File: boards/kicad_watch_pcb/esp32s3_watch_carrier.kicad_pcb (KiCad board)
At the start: 2 copper layers, 180 x 120 mm, 10 parts, among them J1 ESP32-S3 GPIO BUS, J2 ST7735 128x128, J3 I2S MIC, J4 MAX98357A, J5 MPU6050, J6 POWER, SW1 P4, SW2 P5, SW3 P6, SW4 P7

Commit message: Route KiCad watch signal traces
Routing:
- net GPIO12_TFT_SCK: track 0.00 -> 170.5 mm
- net GPIO15_TFT_LED: track 0.00 -> 155.0 mm
- net GPIO11_TFT_MOSI: track 0.00 -> 146.5 mm
- net GPIO8_TFT_RST: track 0.00 -> 135.5 mm
- net GPIO17_I2S_WS: track 0.00 -> 134.4 mm
- net GPIO16_I2S_BCLK: track 0.00 -> 134.4 mm
- net GPIO14_SPK_DIN: track 0.00 -> 96.4 mm
- net GPIO9_TFT_DC: track 0.00 -> 84.7 mm
- net GPIO10_TFT_CS: track 0.00 -> 84.7 mm
- net GPIO18_MIC_SD: track 0.00 -> 72.0 mm
- net GPIO42_MPU_SDA: track 0.00 -> 65.1 mm
- net GPIO41_MPU_SCL: track 0.00 -> 65.1 mm
- net GPIO13_MPU_INT: track 0.00 -> 65.1 mm
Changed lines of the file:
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@@
     (effects (font (size 0.9 0.9) (thickness 0.12)))
   )
+  (segment (start 96.00 61.02) (end 86.00 61.02) (width 0.25) (layer "B.Cu") (net 14))
+  (segment (start 86.00 61.02) (end 86.00 75.00) (width 0.25) (layer "B.Cu") (net 14))
+  (segment (start 86.00 75.00) (end 14.00 75.00) (width 0.25) (layer "B.Cu") (net 14))
+  (segment (start 14.00 75.00) (end 14.00 27.00) (width 0.25) (layer "B.Cu") (net 14))
+  (segment (start 14.00 27.00) (end 25.00 27.00) (width 0.25) (layer "B.Cu") (net 14))
+  (segment (start 96.00 55.94) (end 120.00 55.94) (width 0.25) (layer "F.Cu") (net 12))
+  (segment (start 120.00 55.94) (end 120.00 20.00) (width 0.25) (layer "F.Cu") (net 12))
+  (segment (start 120.00 20.00) (end 22.00 20.00) (width 0.25) (layer "F.Cu") (net 12))
+  (segment (start 22.00 20.00) (end 22.00 29.54) (width 0.25) (layer "F.Cu") (net 12))
+  (segment (start 22.00 29.54) (end 25.00 29.54) (width 0.25) (layer "F.Cu") (net 12))
+  (segment (start 96.00 53.40) (end 115.00 53.40) (width 0.25) (layer "F.Cu") (net 11))
+  (segment (start 115.00 53.40) (end 115.00 24.00) (width 0.25) (layer "F.Cu") (net 11))
+  (segment (start 115.00 24.00) (end 30.00 24.00) (width 0.25) (layer "F.Cu") (net 11))
+  (segment (start 30.00 24.00) (end 30.00 32.08) (width 0.25) (layer "F.Cu") (net 11))
+  (segment (start 30.00 32.08) (end 25.00 32.08) (width 0.25) (layer "F.Cu") (net 11))
+  (segment (start 96.00 48.32) (end 75.00 48.32) (width 0.25) (layer "F.Cu") (net 9))
+  (segment (start 75.00 48.32) (end 75.00 34.62) (width 0.25) (layer "F.Cu") (net 9))
+  (segment (start 75.00 34.62) (end 25.00 34.62) (width 0.25) (layer "F.Cu") (net 9))
+  (segment (start 96.00 50.86) (end 65.00 50.86) (width 0.25) (layer "F.Cu") (net 10))
+  (segment (start 65.00 50.86) (end 65.00 37.16) (width 0.25) (layer "F.Cu") (net 10))
+  (segment (start 65.00 37.16) (end 25.00 37.16) (width 0.25) (layer "F.Cu") (net 10))
+  (segment (start 96.00 45.78) (end 80.00 45.78) (width 0.25) (layer "B.Cu") (net 8))
+  (segment (start 80.00 45.78) (end 80.00 70.00) (width 0.25) (layer "B.Cu") (net 8))
+  (segment (start 80.00 70.00) (end 20.00 70.00) (width 0.25) (layer "B.Cu") (net 8))
+  (segment (start 20.00 70.00) (end 20.00 39.70) (width 0.25) (layer "B.Cu") (net 8))
+  (segment (start 20.00 39.70) (end 25.00 39.70) (width 0.25) (layer "B.Cu") (net 8))
+  (segment (start 96.00 63.56) (end 158.00 27.00) (width 0.25) (layer "B.Cu") (net 15))
+  (segment (start 96.00 66.10) (end 158.00 29.54) (width 0.25) (layer "B.Cu") (net 16))
+  (segment (start 96.00 68.64) (end 158.00 32.08) (width 0.25) (layer "B.Cu") (net 17))
+  (segment (start 96.00 63.56) (end 158.00 56.00) (width 0.25) (layer "F.Cu") (net 15))
+  (segment (start 96.00 66.10) (end 158.00 58.54) (width 0.25) (layer "F.Cu") (net 16))
+  (segment (start 96.00 58.48) (end 94.00 58.48) (width 0.25) (layer "F.Cu") (net 13))
+  (segment (start 94.00 58.48) (end 94.00 75.00) (width 0.25) (layer "F.Cu") (net 13))
+  (segment (start 94.00 75.00) (end 152.00 75.00) (width 0.25) (layer "F.Cu") (net 13))
+  (segment (start 152.00 75.00) (end 152.00 61.08) (width 0.25) (layer "F.Cu") (net 13))
+  (segment (start 152.00 61.08) (end 158.00 61.08) (width 0.25) (layer "F.Cu") (net 13))
+  (segment (start 96.00 71.18) (end 158.00 91.08) (width 0.25) (layer "B.Cu") (net 18))
+  (segment (start 96.00 73.72) (end 158.00 93.62) (width 0.25) (layer "B.Cu") (net 19))
+  (segment (start 96.00 76.26) (end 158.00 96.16) (width 0.25) (layer "B.Cu") (net 20))
 )

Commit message: Refine KiCad signal routing
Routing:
- net GPIO17_I2S_WS: track 134.4 -> 168.1 mm
- net GPIO16_I2S_BCLK: track 134.4 -> 168.1 mm
- net GPIO18_MIC_SD: track 72.0 -> 98.6 mm
- net GPIO42_MPU_SDA: track 65.1 -> 81.9 mm
- net GPIO41_MPU_SCL: track 65.1 -> 81.9 mm
- net GPIO13_MPU_INT: track 65.1 -> 81.9 mm
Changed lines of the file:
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@@
   (segment (start 20.00 70.00) (end 20.00 39.70) (width 0.25) (layer "B.Cu") (net 8))
   (segment (start 20.00 39.70) (end 25.00 39.70) (width 0.25) (layer "B.Cu") (net 8))
-  (segment (start 96.00 63.56) (end 158.00 27.00) (width 0.25) (layer "B.Cu") (net 15))
-  (segment (start 96.00 66.10) (end 158.00 29.54) (width 0.25) (layer "B.Cu") (net 16))
-  (segment (start 96.00 68.64) (end 158.00 32.08) (width 0.25) (layer "B.Cu") (net 17))
-  (segment (start 96.00 63.56) (end 158.00 56.00) (width 0.25) (layer "F.Cu") (net 15))
-  (segment (start 96.00 66.10) (end 158.00 58.54) (width 0.25) (layer "F.Cu") (net 16))
+  (segment (start 96.00 63.56) (end 125.00 63.56) (width 0.25) (layer "B.Cu") (net 15))
+  (segment (start 125.00 63.56) (end 125.00 27.00) (width 0.25) (layer "B.Cu") (net 15))
+  (segment (start 125.00 27.00) (end 158.00 27.00) (width 0.25) (layer "B.Cu") (net 15))
+  (segment (start 96.00 66.10) (end 130.00 66.10) (width 0.25) (layer "B.Cu") (net 16))
+  (segment (start 130.00 66.10) (end 130.00 29.54) (width 0.25) (layer "B.Cu") (net 16))
+  (segment (start 130.00 29.54) (end 158.00 29.54) (width 0.25) (layer "B.Cu") (net 16))
+  (segment (start 96.00 68.64) (end 135.00 68.64) (width 0.25) (layer "B.Cu") (net 17))
+  (segment (start 135.00 68.64) (end 135.00 32.08) (width 0.25) (layer "B.Cu") (net 17))
+  (segment (start 135.00 32.08) (end 158.00 32.08) (width 0.25) (layer "B.Cu") (net 17))
+  (segment (start 96.00 63.56) (end 125.00 63.56) (width 0.25) (layer "F.Cu") (net 15))
+  (segment (start 125.00 63.56) (end 125.00 56.00) (width 0.25) (layer "F.Cu") (net 15))
+  (segment (start 125.00 56.00) (end 158.00 56.00) (width 0.25) (layer "F.Cu") (net 15))
+  (segment (start 96.00 66.10) (end 130.00 66.10) (width 0.25) (layer "F.Cu") (net 16))
+  (segment (start 130.00 66.10) (end 130.00 58.54) (width 0.25) (layer "F.Cu") (net 16))
+  (segment (start 130.00 58.54) (end 158.00 58.54) (width 0.25) (layer "F.Cu") (net 16))
   (segment (start 96.00 58.48) (end 94.00 58.48) (width 0.25) (layer "F.Cu") (net 13))
   (segment (start 94.00 58.48) (end 94.00 75.00) (width 0.25) (layer "F.Cu") (net 13))
@@
   (segment (start 152.00 75.00) (end 152.00 61.08) (width 0.25) (layer "F.Cu") (net 13))
   (segment (start 152.00 61.08) (end 158.00 61.08) (width 0.25) (layer "F.Cu") (net 13))
-  (segment (start 96.00 71.18) (end 158.00 91.08) (width 0.25) (layer "B.Cu") (net 18))
-  (segment (start 96.00 73.72) (end 158.00 93.62) (width 0.25) (layer "B.Cu") (net 19))
-  (segment (start 96.00 76.26) (end 158.00 96.16) (width 0.25) (layer "B.Cu") (net 20))
+  (segment (start 96.00 71.18) (end 154.00 71.18) (width 0.25) (layer "B.Cu") (net 18))
+  (segment (start 154.00 71.18) (end 154.00 91.08) (width 0.25) (layer "B.Cu") (net 18))
+  (segment (start 154.00 91.08) (end 158.00 91.08) (width 0.25) (layer "B.Cu") (net 18))
+  (segment (start 96.00 73.72) (end 151.00 73.72) (width 0.25) (layer "B.Cu") (net 19))
+  (segment (start 151.00 73.72) (end 151.00 93.62) (width 0.25) (layer "B.Cu") (net 19))
+  (segment (start 151.00 93.62) (end 158.00 93.62) (width 0.25) (layer "B.Cu") (net 19))
+  (segment (start 96.00 76.26) (end 148.00 76.26) (width 0.25) (layer "B.Cu") (net 20))
+  (segment (start 148.00 76.26) (end 148.00 96.16) (width 0.25) (layer "B.Cu") (net 20))
+  (segment (start 148.00 96.16) (end 158.00 96.16) (width 0.25) (layer "B.Cu") (net 20))
 )

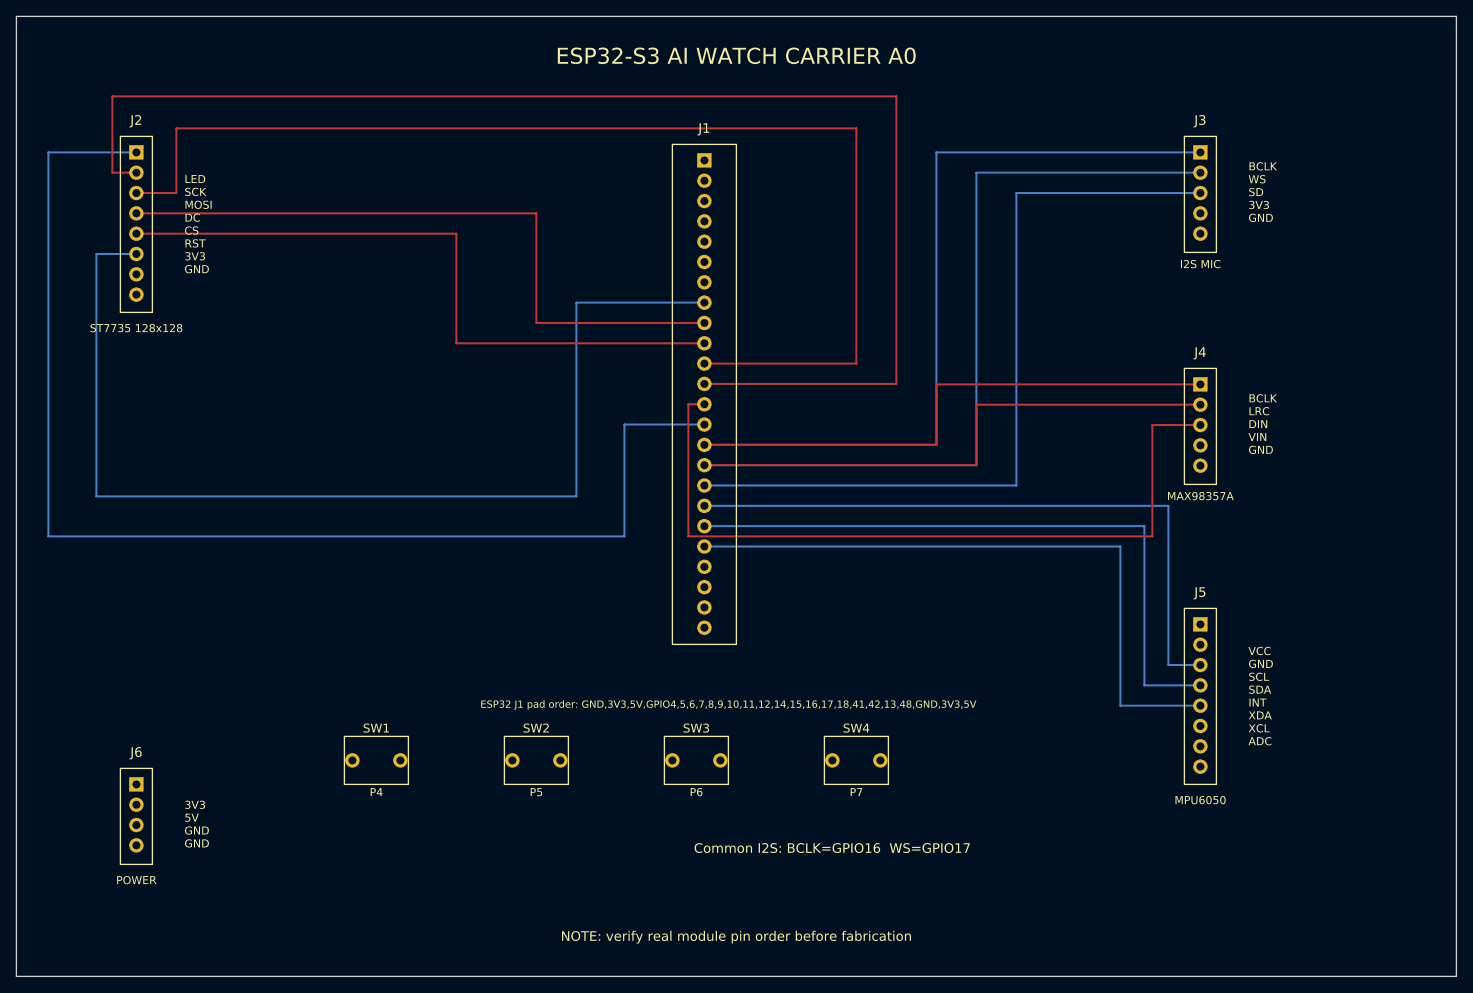
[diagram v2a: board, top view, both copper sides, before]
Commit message: Complete KiCad carrier routing
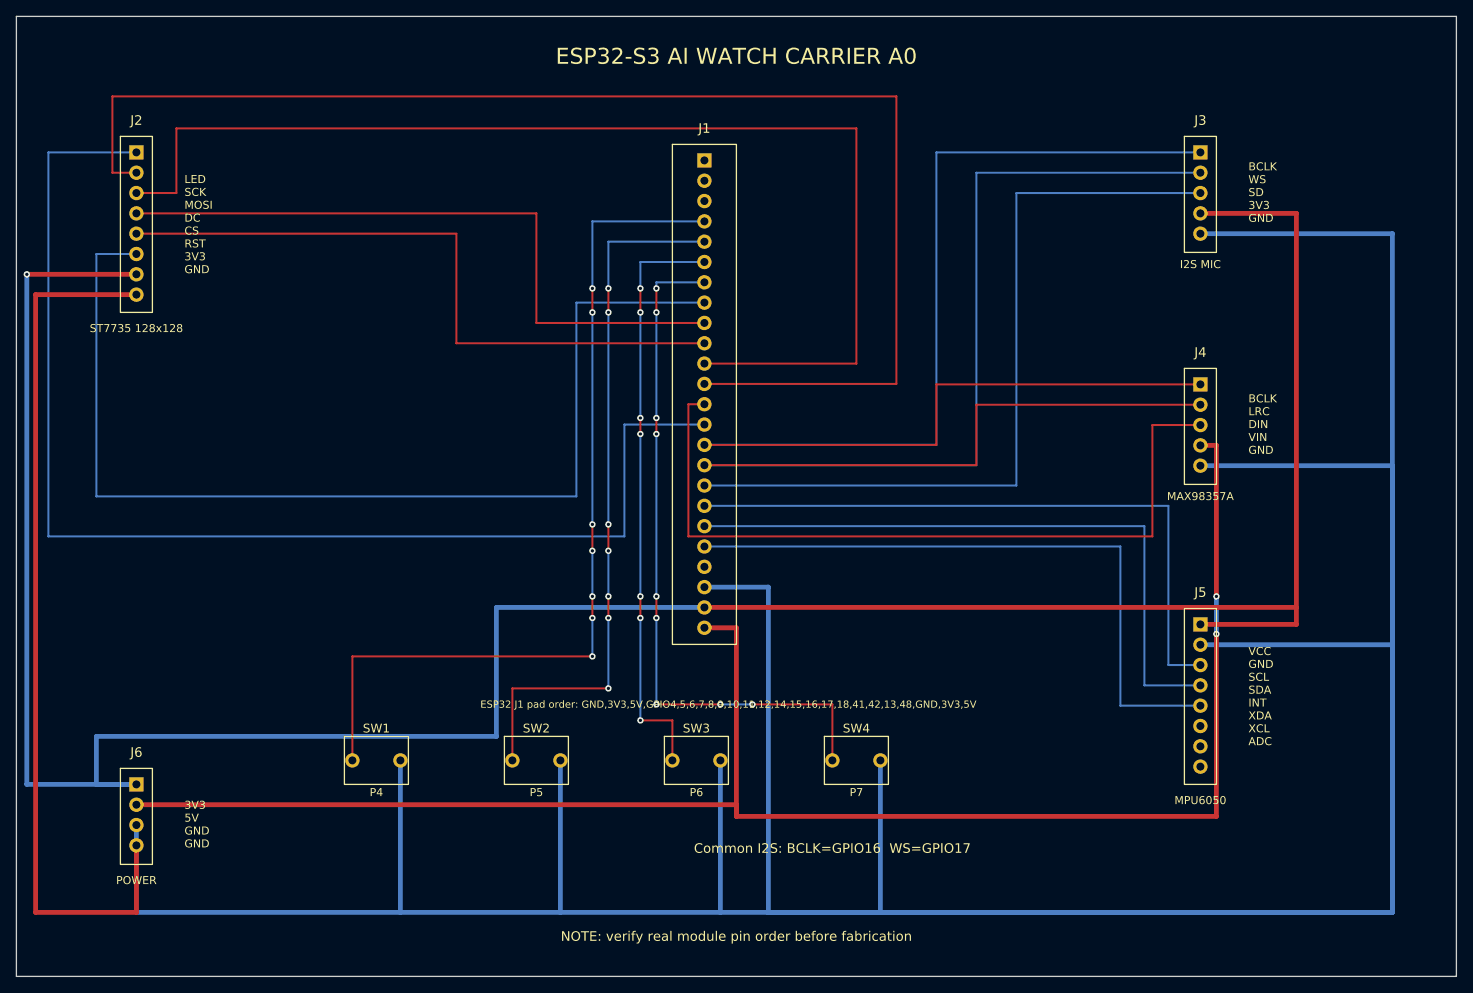
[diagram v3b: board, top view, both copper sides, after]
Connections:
- J1 pad 1: GND -> (no net)
- J1 pad 2: 3V3 -> (no net)
- J1 pad 3: 5V -> (no net)
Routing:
- net GND: track 0.00 -> 819.5 mm
- net 3V3: track 0.00 -> 343.7 mm, vias 0 -> 1
- net 5V: track 0.00 -> 212.4 mm, vias 0 -> 2
- net GPIO4_P4: track 0.00 -> 111.4 mm, vias 0 -> 7
- net GPIO5_P5: track 0.00 -> 88.8 mm, vias 0 -> 7
- net GPIO7_P7: track 0.00 -> 87.8 mm, vias 0 -> 9
- net GPIO6_P6: track 0.00 -> 74.3 mm, vias 0 -> 7

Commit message: Add carrier decoupling footprints
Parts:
- added C1: 100nF TFT, C_0805_WATCH, F.Cu at (19.0, 43.5)
- added C2: 100nF MIC, C_0805_WATCH, F.Cu at (150.0, 35.9)
- added C3: 100nF AMP, C_0805_WATCH, F.Cu at (163.0, 64.9)
- added C4: 100nF MPU, C_0805_WATCH, F.Cu at (150.0, 87.3)
- added C5: 10uF IN, C_0805_WATCH, F.Cu at (40.0, 109.8)
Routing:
- net GND: track 819.5 -> 881.5 mm, vias 0 -> 1
- net 3V3: track 343.7 -> 372.5 mm
- net 5V: track 212.4 -> 232.7 mm
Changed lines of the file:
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@@
     (effects (font (size 0.9 0.9) (thickness 0.12)))
+  )
+  (footprint "C_0805_WATCH" (layer "F.Cu")
+    (at 19.00 43.50)
+    (attr smd)
+    (fp_text reference "C1" (at 0 -1.8) (layer "F.SilkS") (effects (font (size 0.8 0.8) (thickness 0.12))))
+    (fp_text value "100nF TFT" (at 0 1.8) (layer "F.Fab") (effects (font (size 0.7 0.7) (thickness 0.1))))
+    (fp_rect (start -1.8 -0.9) (end 1.8 0.9) (layer "F.SilkS") (width 0.10))
+    (pad "1" smd rect (at -1.00 0) (size 1.20 1.30) (layers "F.Cu" "F.Paste" "F.Mask") (net 2 "3V3"))
+    (pad "2" smd rect (at 1.00 0) (size 1.20 1.30) (layers "F.Cu" "F.Paste" "F.Mask") (net 1 "GND"))
+  )
+  (footprint "C_0805_WATCH" (layer "F.Cu")
+    (at 150.00 35.90)
+    (attr smd)
+    (fp_text reference "C2" (at 0 -1.8) (layer "F.SilkS") (effects (font (size 0.8 0.8) (thickness 0.12))))
+    (fp_text value "100nF MIC" (at 0 1.8) (layer "F.Fab") (effects (font (size 0.7 0.7) (thickness 0.1))))
+    (fp_rect (start -1.8 -0.9) (end 1.8 0.9) (layer "F.SilkS") (width 0.10))
+    (pad "1" smd rect (at -1.00 0) (size 1.20 1.30) (layers "F.Cu" "F.Paste" "F.Mask") (net 2 "3V3"))
+    (pad "2" smd rect (at 1.00 0) (size 1.20 1.30) (layers "F.Cu" "F.Paste" "F.Mask") (net 1 "GND"))
+  )
+  (footprint "C_0805_WATCH" (layer "F.Cu")
+    (at 163.00 64.90 270)
+    (attr smd)
+    (fp_text reference "C3" (at 0 -1.8) (layer "F.Fab") (effects (font (size 0.8 0.8) (thickness 0.12))))
+    (fp_text value "100nF AMP" (at 0 1.8) (layer "F.Fab") (effects (font (size 0.7 0.7) (thickness 0.1))))
+    (fp_rect (start -1.8 -0.9) (end 1.8 0.9) (layer "F.SilkS") (width 0.10))
+    (pad "1" smd rect (at -1.00 0) (size 1.20 1.30) (layers "F.Cu" "F.Paste" "F.Mask") (net 3 "5V"))
+    (pad "2" smd rect (at 1.00 0) (size 1.20 1.30) (layers "F.Cu" "F.Paste" "F.Mask") (net 1 "GND"))
+  )
+  (footprint "C_0805_WATCH" (layer "F.Cu")
+    (at 150.00 87.30)
+    (attr smd)
+    (fp_text reference "C4" (at 0 -1.8) (layer "F.SilkS") (effects (font (size 0.8 0.8) (thickness 0.12))))
+    (fp_text value "100nF MPU" (at 0 1.8) (layer "F.Fab") (effects (font (size 0.7 0.7) (thickness 0.1))))
+    (fp_rect (start -1.8 -0.9) (end 1.8 0.9) (layer "F.SilkS") (width 0.10))
+    (pad "1" smd rect (at -1.00 0) (size 1.20 1.30) (layers "F.Cu" "F.Paste" "F.Mask") (net 2 "3V3"))
+    (pad "2" smd rect (at 1.00 0) (size 1.20 1.30) (layers "F.Cu" "F.Paste" "F.Mask") (net 1 "GND"))
+  )
+  (footprint "C_0805_WATCH" (layer "F.Cu")
+    (at 40.00 109.80)
+    (attr smd)
+    (fp_text reference "C5" (at 0 -1.8) (layer "F.SilkS") (effects (font (size 0.8 0.8) (thickness 0.12))))
+    (fp_text value "10uF IN" (at 0 1.8) (layer "F.Fab") (effects (font (size 0.7 0.7) (thickness 0.1))))
+    (fp_rect (start -1.8 -0.9) (end 1.8 0.9) (layer "F.SilkS") (width 0.10))
+    (pad "1" smd rect (at -1.00 0) (size 1.20 1.30) (layers "F.Cu" "F.Paste" "F.Mask") (net 3 "5V"))
+    (pad "2" smd rect (at 1.00 0) (size 1.20 1.30) (layers "F.Cu" "F.Paste" "F.Mask") (net 1 "GND"))
   )
   (segment (start 96.00 61.02) (end 86.00 61.02) (width 0.25) (layer "B.Cu") (net 14))
@@
   (segment (start 102.00 96.00) (end 112.00 96.00) (width 0.25) (layer "F.Cu") (net 7))
   (segment (start 112.00 96.00) (end 112.00 103.00) (width 0.25) (layer "F.Cu") (net 7))
+  (segment (start 18.00 43.50) (end 18.00 42.24) (width 0.25) (layer "F.Cu") (net 2))
+  (segment (start 18.00 42.24) (end 25.00 42.24) (width 0.25) (layer "F.Cu") (net 2))
+  (segment (start 20.00 43.50) (end 20.00 44.78) (width 0.25) (layer "F.Cu") (net 1))
+  (segment (start 20.00 44.78) (end 25.00 44.78) (width 0.25) (layer "F.Cu") (net 1))
+  (segment (start 149.00 35.90) (end 149.00 34.62) (width 0.25) (layer "F.Cu") (net 2))
+  (segment (start 149.00 34.62) (end 158.00 34.62) (width 0.25) (layer "F.Cu") (net 2))
+  (segment (start 151.00 35.90) (end 151.00 37.16) (width 0.25) (layer "F.Cu") (net 1))
+  (segment (start 151.00 37.16) (end 158.00 37.16) (width 0.25) (layer "F.Cu") (net 1))
+  (segment (start 149.00 87.30) (end 149.00 86.00) (width 0.25) (layer "F.Cu") (net 2))
+  (segment (start 149.00 86.00) (end 158.00 86.00) (width 0.25) (layer "F.Cu") (net 2))
+  (segment (start 151.00 87.30) (end 151.00 88.54) (width 0.25) (layer "F.Cu") (net 1))
+  (segment (start 151.00 88.54) (end 158.00 88.54) (width 0.25) (layer "F.Cu") (net 1))
+  (segment (start 39.00 109.80) (end 39.00 108.54) (width 0.35) (layer "F.Cu") (net 3))
+  (segment (start 39.00 108.54) (end 25.00 108.54) (width 0.35) (layer "F.Cu") (net 3))
+  (segment (start 41.00 109.80) (end 41.00 111.08) (width 0.35) (layer "F.Cu") (net 1))
+  (segment (start 41.00 111.08) (end 25.00 111.08) (width 0.35) (layer "F.Cu") (net 1))
+  (segment (start 163.00 63.90) (end 158.00 63.62) (width 0.25) (layer "F.Cu") (net 3))
+  (segment (start 163.00 65.90) (end 163.00 67.50) (width 0.25) (layer "F.Cu") (net 1))
+  (via (at 163.00 67.50) (size 0.80) (drill 0.40) (layers "F.Cu" "B.Cu") (net 1))
+  (segment (start 163.00 67.50) (end 182.00 67.50) (width 0.25) (layer "B.Cu") (net 1))
+  (segment (start 182.00 67.50) (end 182.00 66.16) (width 0.25) (layer "B.Cu") (net 1))
 )
